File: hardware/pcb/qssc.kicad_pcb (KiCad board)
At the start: 6 copper layers, 210 x 140 mm, 126 parts, among them J1 FT232RL, J10 USB-C, J12 BTB_HOST, J2 5V Barrel, J3 SMA, J4 12V LED, J7 RESET, J8 MW_GATE, J9 JTAG, U1 XC7A35T-1CSG324C, U3 ADF4351BCPZ, U5 GVA-84+, U8 W25Q128JVSIQ, Y1 100MHz XO

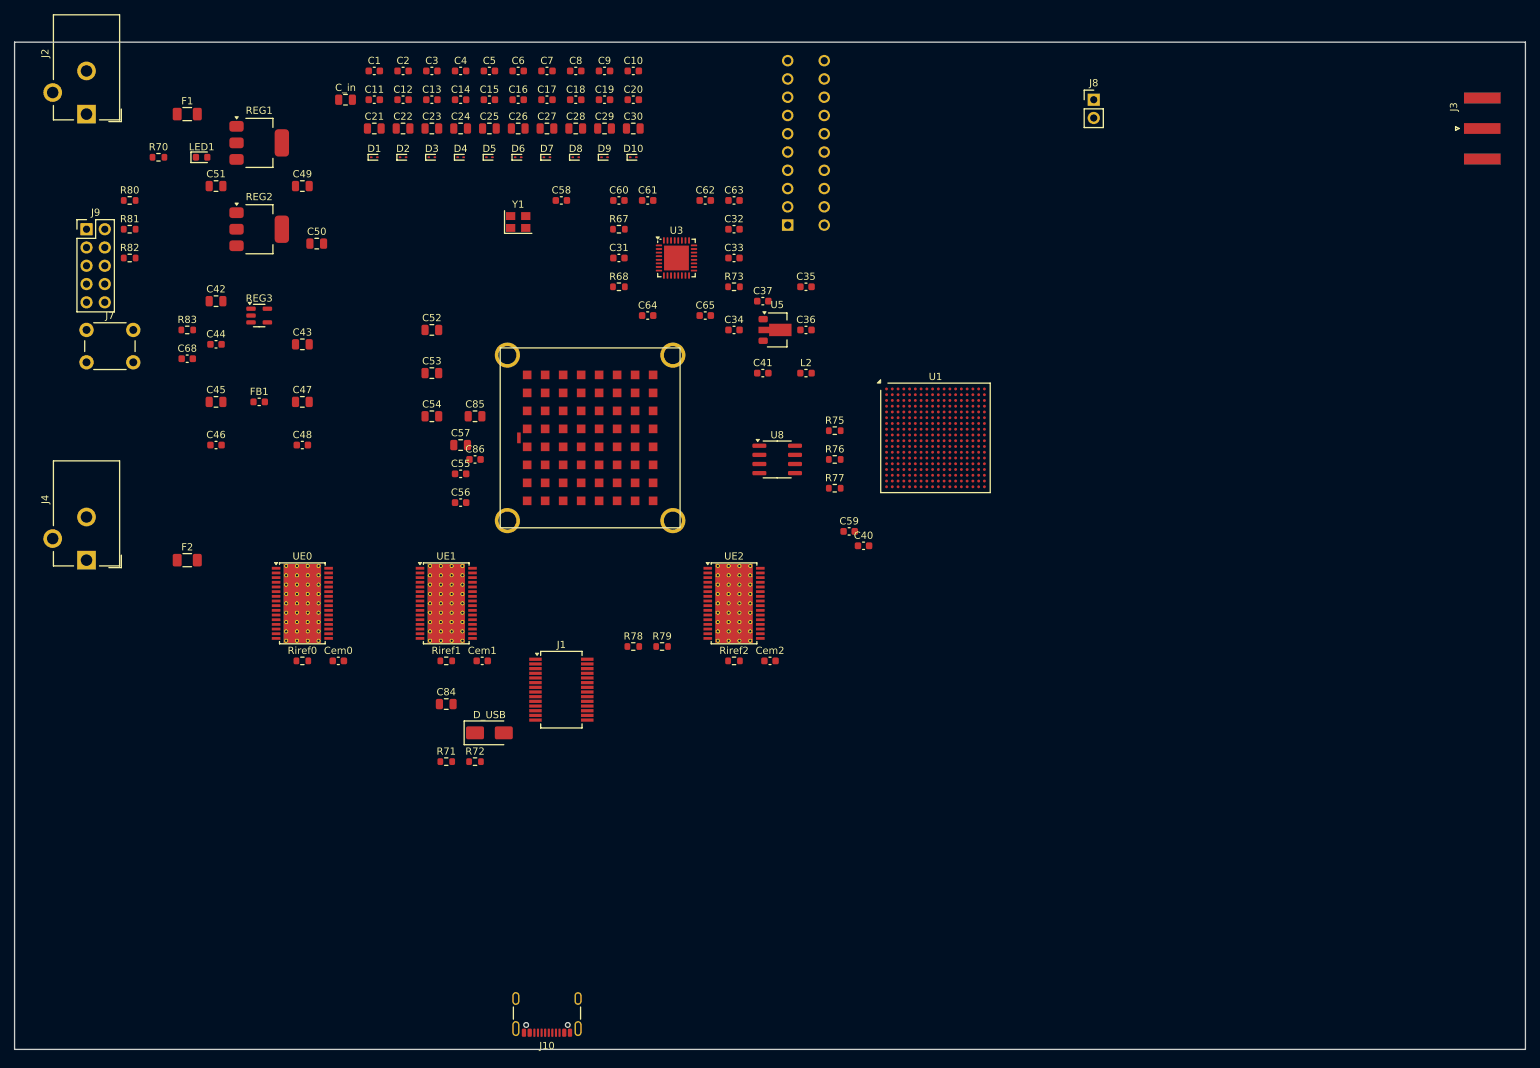
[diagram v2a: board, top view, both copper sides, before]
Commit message: pcb(main): FreeRouting cycle 1 — 96/114 signal nets routed (+952 tracks), 18 unrouted
Incremental-cycle autoroute (MP=4, headless, resource-capped). 711 DRC
violations frozen across all 4 passes (optimizer 0% improvement) — under
investigation, likely in pre-routed fanout copper. Board saved + committed
to preserve progress (no-data-loss policy).

Co-Authored-By: Claude Code <noreply@anthropic.com>
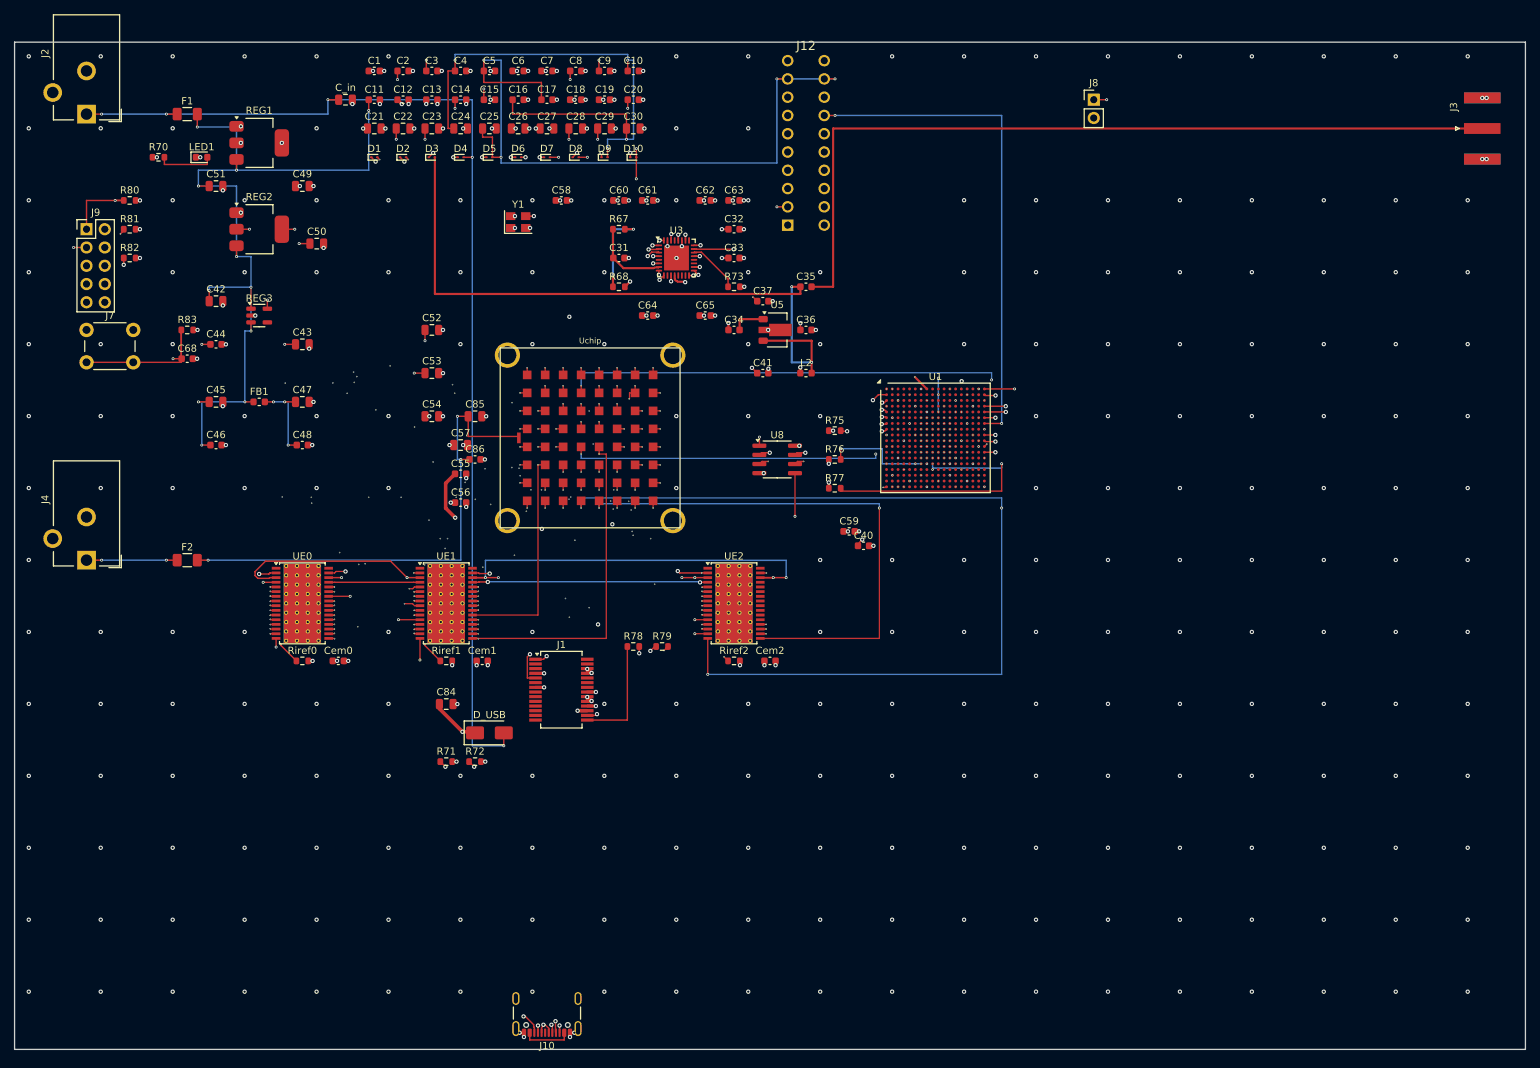
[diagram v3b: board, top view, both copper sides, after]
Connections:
- U3 pad : GND -> (no net)
- UE0 pad : GND -> (no net)
- UE1 pad : GND -> (no net)
- UE2 pad : GND -> (no net)
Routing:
- net +1V0: track 0.00 -> 255.6 mm, vias 0 -> 26
- net +5V: track 0.00 -> 238.4 mm, vias 0 -> 15
- net +1V8: track 0.00 -> 221.6 mm, vias 0 -> 16
- net emitter_cat11: track 0.00 -> 198.6 mm, vias 0 -> 3
- net +5V_RF: track 0.00 -> 189.9 mm, vias 0 -> 8
- net USB_DP: track 0.00 -> 183.6 mm, vias 0 -> 3
- net +5V_IN: track 0.00 -> 155.8 mm, vias 0 -> 5
- net TCK: track 0.00 -> 154.6 mm, vias 0 -> 3
- net mw_gate: track 0.00 -> 151.8 mm, vias 0 -> 4
- net USB_DM: track 0.00 -> 150.7 mm, vias 0 -> 4
- net emitter_cat35: track 0.00 -> 147.7 mm, vias 0 -> 3
- net TDO: track 0.00 -> 147.3 mm, vias 0 -> 2
- net emitter_cat59: track 0.00 -> 131.2 mm, vias 0 -> 3
- net reset: track 0.00 -> 128.3 mm, vias 0 -> 2
- net em_xlat: track 0.00 -> 116.6 mm, vias 0 -> 6
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- added copper zone on In2.Cu, net +3V3
- added copper zone on In1.Cu, net GND

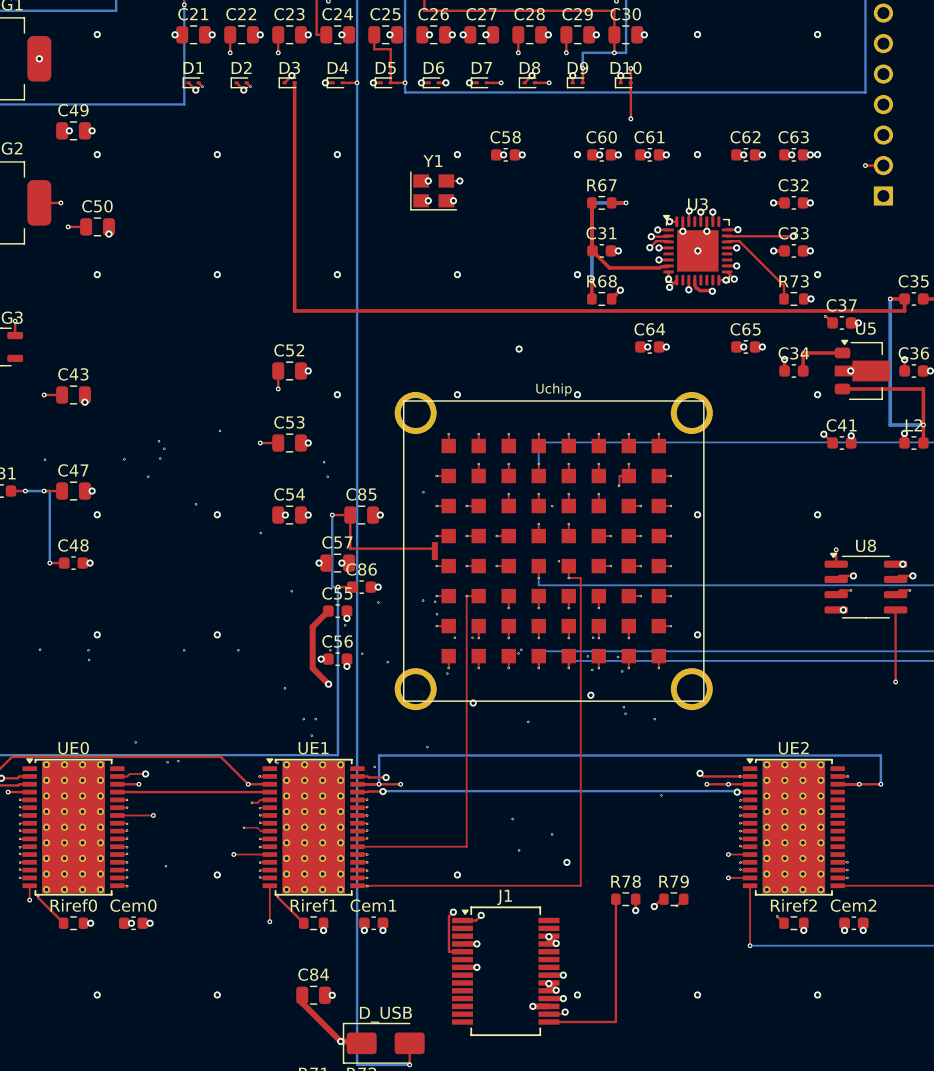
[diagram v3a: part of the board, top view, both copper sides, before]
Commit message: pcb(main): re-pour planes + lower Chip track_width to 0.10mm HDI floor → DRC 0
Re-pouring after autoroute carved clearance around FreeRouting's 952 new
tracks/vias → fixed 700 zone/hole-clearance violations. The remaining 76
were emitter_cat dog-bone stubs FreeRouting auto-narrowed to 0.112 mm to
fit the 0.30 mm-pitch die field; lowering the Chip netclass + global
min_track_width to 0.10 mm (HDI 4-mil floor) makes them legal. kicad-cli
pcb drc: 0 violations, 0 unconnected (18 signal nets still unrouted, gated
by unconnected_items=ignore — cycle 2 next). Generator + project both fixed.

Co-Authored-By: Claude Code <noreply@anthropic.com>
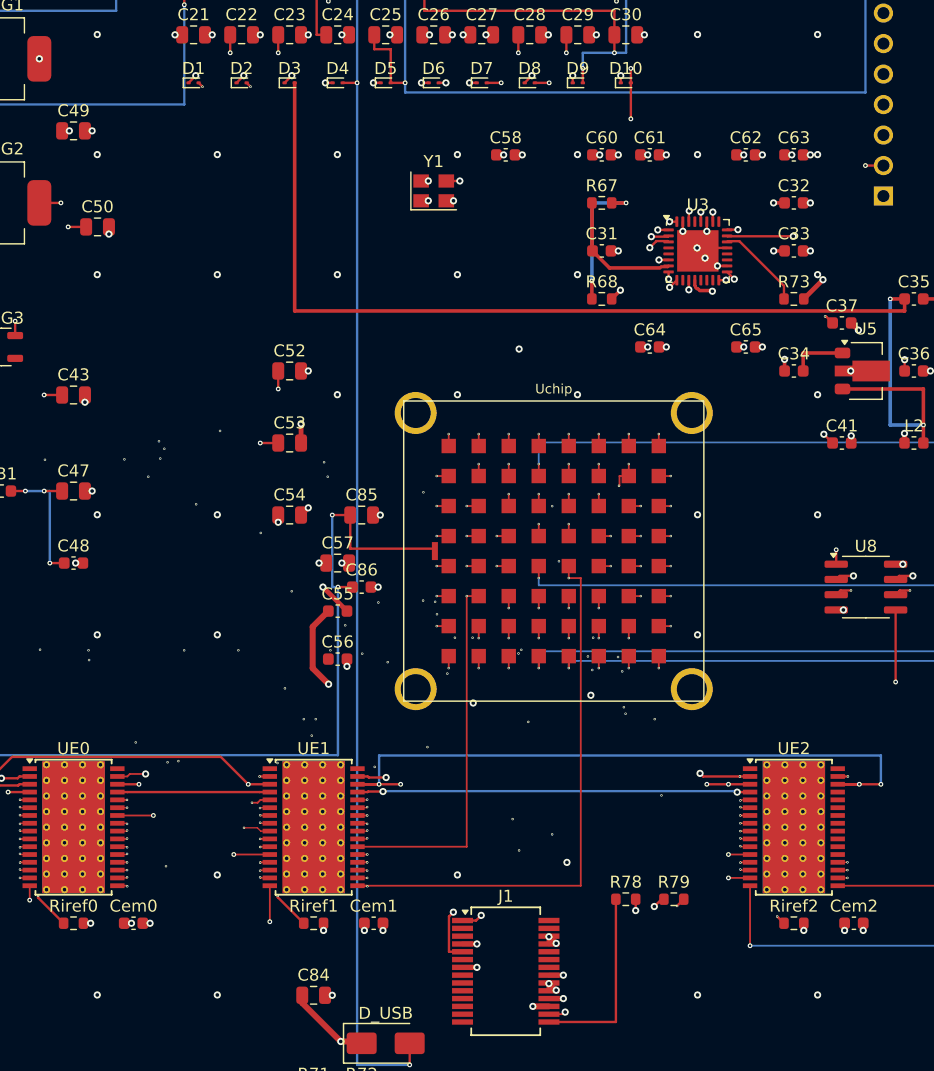
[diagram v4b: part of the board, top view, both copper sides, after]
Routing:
- net GND: track 73.5 -> 81.4 mm, vias 403 -> 402
- net +3V3: track 29.9 -> 28.5 mm, vias 76 -> 74
